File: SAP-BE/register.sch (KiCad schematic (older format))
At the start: 11 parts, among them U7 74LS173, U8 74LS173, U9 74LS245

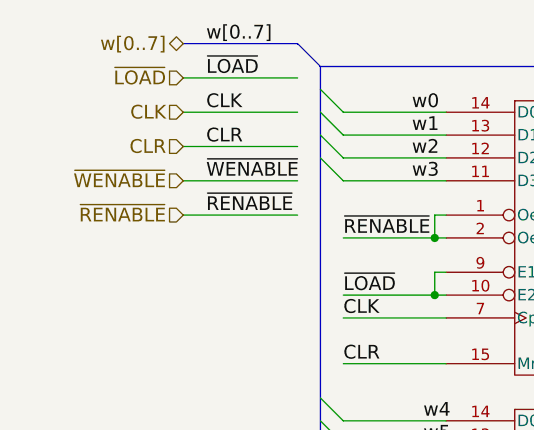
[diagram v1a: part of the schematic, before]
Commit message: Update with changes for reset
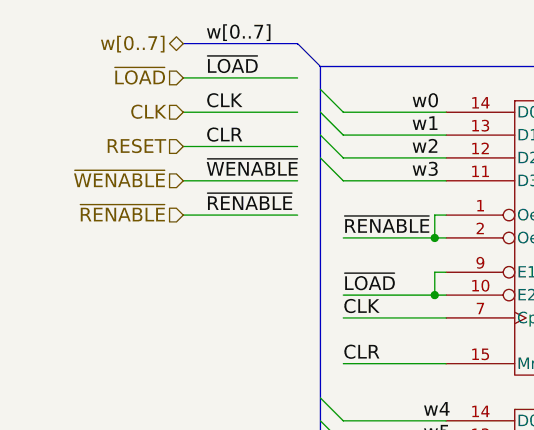
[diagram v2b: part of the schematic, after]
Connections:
- net labels added: RESET
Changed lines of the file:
@@
 $Descr A4 11693 8268
 encoding utf-8
-Sheet 5 11
+Sheet 4 11
 Title "Simple As Possible computer by Ben Eater"
 Date "2017-05-10"
@@
 Text HLabel 3100 2350 0    60   Input ~ 0
 ~RENABLE
-Text HLabel 3100 2050 0    60   Input ~ 0
-CLR
 Text HLabel 3100 1750 0    60   Input ~ 0
 ~LOAD
@@
 ~LOAD
 $Comp
-L GND #PWR25
+L GND #PWR025
 U 1 1 591439AA
 P 8650 4700
-AR Path="/590AA801/591439AA" Ref="#PWR25"  Part="1"
-AR Path="/590A2A35/591439AA" Ref="#PWR27"  Part="1"
-F 0 "#PWR27" H 8650 4450 50  0001 C CNN
+AR Path="/590AA801/591439AA" Ref="#PWR025"  Part="1"
+AR Path="/590A2A35/591439AA" Ref="#PWR027"  Part="1"
+F 0 "#PWR027" H 8650 4450 50  0001 C CNN
 F 1 "GND" H 8650 4550 50  0000 C CNN
 F 2 "" H 8650 4700 50  0000 C CNN
@@
 	3600 1600 3100 1600
 $Comp
-L VCC #PWR26
+L VCC #PWR028
 U 1 1 59141563
 P 6550 3400
-AR Path="/590A2A35/59141563" Ref="#PWR26"  Part="1"
-AR Path="/590AA801/59141563" Ref="#PWR24"  Part="1"
-F 0 "#PWR26" H 6550 3250 50  0001 C CNN
+AR Path="/590A2A35/59141563" Ref="#PWR028"  Part="1"
+AR Path="/590AA801/59141563" Ref="#PWR026"  Part="1"
+F 0 "#PWR028" H 6550 3250 50  0001 C CNN
 F 1 "VCC" H 6550 3550 50  0000 C CNN
 F 2 "" H 6550 3400 50  0000 C CNN
@@
 Text Label 8100 3200 0    60   ~ 0
 w7
+Text HLabel 3100 2050 0    60   Input ~ 0
+RESET
 $EndSCHEMATC
